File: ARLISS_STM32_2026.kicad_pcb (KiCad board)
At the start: 2 copper layers, 32 parts, among them J1 Conn_01x06, J2 Conn_01x06, U14 XL4005, U15 XC6220B331MR, U3 4754

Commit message: AVANCE 06
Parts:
- added SW1: SWITCH_BLACK, ARLISS-footprints:SW-TH_XKB_SS-12M11XX, F.Cu at (180.4, 115.3)
- added SW2: SWITCH_BLACK, ARLISS-footprints:SW-TH_XKB_SS-12M11XX, F.Cu at (179.0, 132.9)
- added U16: AP64501SP-13, ARLISS-footprints:SOIC-8_L4.9-W3.9-P1.27-LS6.0-BL-EP-1, F.Cu at (194.2, 100.8)

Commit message: feat: [solución de rules checker]
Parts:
- U14: value XL4005 -> XL4005E1
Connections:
- net GND renamed nFAULT2
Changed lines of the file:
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@@
 			(layers "F.Cu" "F.Mask" "F.Paste")
 			(roundrect_rratio 0.208333)
-			(net "GND")
+			(net "nFAULT2")
 			(pinfunction "A_1")
 			(pintype "passive")
@@
 			(layers "F.Cu" "F.Mask" "F.Paste")
 			(roundrect_rratio 0.208333)
-			(net "GND")
+			(net "nFAULT2")
 			(pinfunction "A_3")
 			(pintype "passive")
@@
 			(layers "F.Cu" "F.Mask" "F.Paste")
 			(roundrect_rratio 0.25)
-			(net "GND")
+			(net "nFAULT2")
 			(pintype "passive")
 		)
@@
 			(layers "F.Cu" "F.Mask" "F.Paste")
 			(roundrect_rratio 0.25)
-			(net "GND")
+			(net "nFAULT2")
 			(pintype "passive")
 		)
@@
 			(layers "F.Cu" "F.Mask" "F.Paste")
 			(roundrect_rratio 0.15625)
-			(net "GND")
+			(net "nFAULT2")
 			(pintype "passive")
 		)
@@
 			(size 1.5 1.5)
 			(layers "F.Cu" "F.Mask")
-			(net "GND")
+			(net "nFAULT2")
 			(pinfunction "1_1")
 			(pintype "passive")
@@
 			(layers "*.Cu" "*.Mask")
 			(remove_unused_layers no)
-			(net "GND")
+			(net "nFAULT2")
 			(pinfunction "Pin_5_5")
 			(pintype "passive")
@@
 			(layers "F.Cu" "F.Mask" "F.Paste")
 			(roundrect_rratio 0.25)
-			(net "GND")
+			(net "nFAULT2")
 			(pintype "passive")
 		)
@@
 			(layers "F.Cu" "F.Mask" "F.Paste")
 			(roundrect_rratio 0.25)
-			(net "GND")
+			(net "nFAULT2")
 			(pintype "passive")
 		)
@@
 			(layers "*.Cu" "*.Mask")
 			(remove_unused_layers no)
-			(net "GND")
+			(net "nFAULT2")
 			(pinfunction "3_3")
 			(pintype "unspecified")
@@
 			(layers "F.Cu" "F.Mask" "F.Paste")
 			(roundrect_rratio 0.25)
-			(net "GND")
+			(net "nFAULT2")
 			(pintype "passive")
 		)
@@
 			(layers "*.Cu" "*.Mask")
 			(remove_unused_layers no)
-			(net "GND")
+			(net "nFAULT2")
 			(pinfunction "Pin_2_2")
 			(pintype "passive")
@@
 			(layers "F.Cu" "F.Mask" "F.Paste")
 			(roundrect_rratio 0.25)
-			(net "GND")
+			(net "nFAULT2")
 			(pintype "passive")
 		)
@@
 			(layers "F.Cu" "F.Mask" "F.Paste")
 			(roundrect_rratio 0.25)
-			(net "GND")
+			(net "nFAULT2")
 			(pintype "passive")
 		)
@@
 			)
 		)
-		(property "Value" "XL4005"
+		(property "Value" "XL4005E1"
 			(at 0 6.65 0)
 			(layer "F.Fab")
@@
 			)
 		)
-		(property "Datasheet" "http://www.xlsemi.net/datasheet/XL4015%20datasheet-English.pdf"
+		(property "Datasheet" "https://lcsc.com/product-detail/DC-DC-Converters_XL4005E1_C73332.html"
 			(at 0 0 0)
 			(layer "F.Fab")
@@
 			)
 		)
-		(property "Description" "5A 180kHz 36V Buck DC to DC Converter"
+		(property "Description" ""
 			(at 0 0 0)
 			(layer "F.Fab")
@@
 			)
 		)
-		(property ki_fp_filters "TO?263*")
+		(property "Manufacturer" "XLSEMI(芯龙)"
+			(at 0 0 0)
+			(unlocked yes)
+			(layer "F.Fab")
+			(hide yes)
+			(effects
+				(font
+					(size 1 1)
+					(thickness 0.15)
+				)
+			)
+		)
+		(property "MPN" "XL4005E1"
+			(at 0 0 0)
+			(unlocked yes)
+			(layer "F.Fab")
+			(hide yes)
+			(effects
+				(font
+					(size 1 1)
+					(thickness 0.15)
+				)
+			)
+		)
+		(property "LCSC Part" "C73332"
+			(at 0 0 0)
+			(unlocked yes)
+			(layer "F.Fab")
+			(hide yes)
+			(effects
+				(font
+					(size 1 1)
+					(thickness 0.15)
+				)
+			)
+		)
 		(sheetname "/Alimentacion/")
 		(sheetfile "untitled.kicad_sch")
@@
 			(unit
 				(name "A")
-				(pins "5" "4" "1" "3" "2")
+				(pins "3" "6" "5" "4" "2" "1")
 			)
 		)
-		(attr smd)
+		(attr smd dnp)
 		(duplicate_pad_numbers_are_jumpers no)
 		(fp_line
@@
 			(layers "F.Cu" "F.Mask" "F.Paste")
 			(roundrect_rratio 0.227273)
-			(net "GND")
+			(net "nFAULT2")
 			(pinfunction "GND_1")
-			(pintype "power_in")
+			(pintype "unspecified")
 		)
 		(pad "2" smd roundrect
@@
 			(net "/Alimentacion/FB")
 			(pinfunction "FB_2")
-			(pintype "input")
+			(pintype "unspecified")
 		)
 		(pad "3" smd roundrect
@@
 			(net "/Alimentacion/SW")
 			(pinfunction "SW_3")
-			(pintype "power_out")
+			(pintype "unspecified")
 		)
 		(pad "3" smd roundrect
@@
 			(net "/Alimentacion/SW")
 			(pinfunction "SW_3")
-			(pintype "power_out")
+			(pintype "unspecified")
 		)
 		(pad "4" smd roundrect
@@
 			(roundrect_rratio 0.227273)
 			(net "+VIN")
-			(pinfunction "VC_4")
-			(pintype "input")
+			(pinfunction "EN_4")
+			(pintype "unspecified")
 		)
 		(pad "5" smd roundrect
@@
 			(net "+VIN")
 			(pinfunction "VIN_5")
-			(pintype "power_in")
+			(pintype "unspecified")
 		)
 		(embedded_fonts no)
@@
 			(layers "*.Cu" "*.Mask")
 			(remove_unused_layers no)
-			(net "GND")
+			(net "nFAULT2")
 			(pinfunction "3_3")
 			(pintype "unspecified")
@@
 			(layers "F.Cu" "F.Mask" "F.Paste")
 			(roundrect_rratio 0.15625)
-			(net "GND")
+			(net "nFAULT2")
 			(pintype "passive")
 		)
@@
 			(layers "F.Cu" "F.Mask" "F.Paste")
 			(roundrect_rratio 0.25)
-			(net "GND")
+			(net "nFAULT2")
 			(pintype "passive")
 		)
@@
 			(layers "F.Cu" "F.Mask" "F.Paste")
 			(roundrect_rratio 0.25)
-			(net "GND")
+			(net "nFAULT2")
 			(pintype "passive")
 		)
@@
 			(net "+5V")
 			(pinfunction "VIN_JP1_1")
-			(pintype "input")
+			(pintype "output")
 			(solder_mask_margin 0.102)
 		)
@@
 			(layers "*.Cu" "*.Mask")
 			(remove_unused_layers no)
-			(net "GND")
+			(net "nFAULT2")
 			(pinfunction "GND_JP1_3")
 			(pintype "power_in")
@@
 			(layers "F.Cu" "F.Mask" "F.Paste")
 			(roundrect_rratio 0.25)
-			(net "GND")
+			(net "nFAULT2")
 			(pintype "passive")
 		)
@@
 			(layers "F.Cu" "F.Mask" "F.Paste")
 			(roundrect_rratio 0.25)
-			(net "GND")
+			(net "nFAULT2")
 			(pinfunction "GND_2")
 			(pintype "power_in")
@@
 			(layers "F.Cu" "F.Mask" "F.Paste")
 			(roundrect_rratio 0.25)
-			(net "GND")
+			(net "nFAULT2")
 			(pintype "passive")
 		)
@@
 			(layers "F.Cu" "F.Mask" "F.Paste")
 			(roundrect_rratio 0.25)
-			(net "GND")
+			(net "nFAULT2")
 			(pintype "passive")
 		)

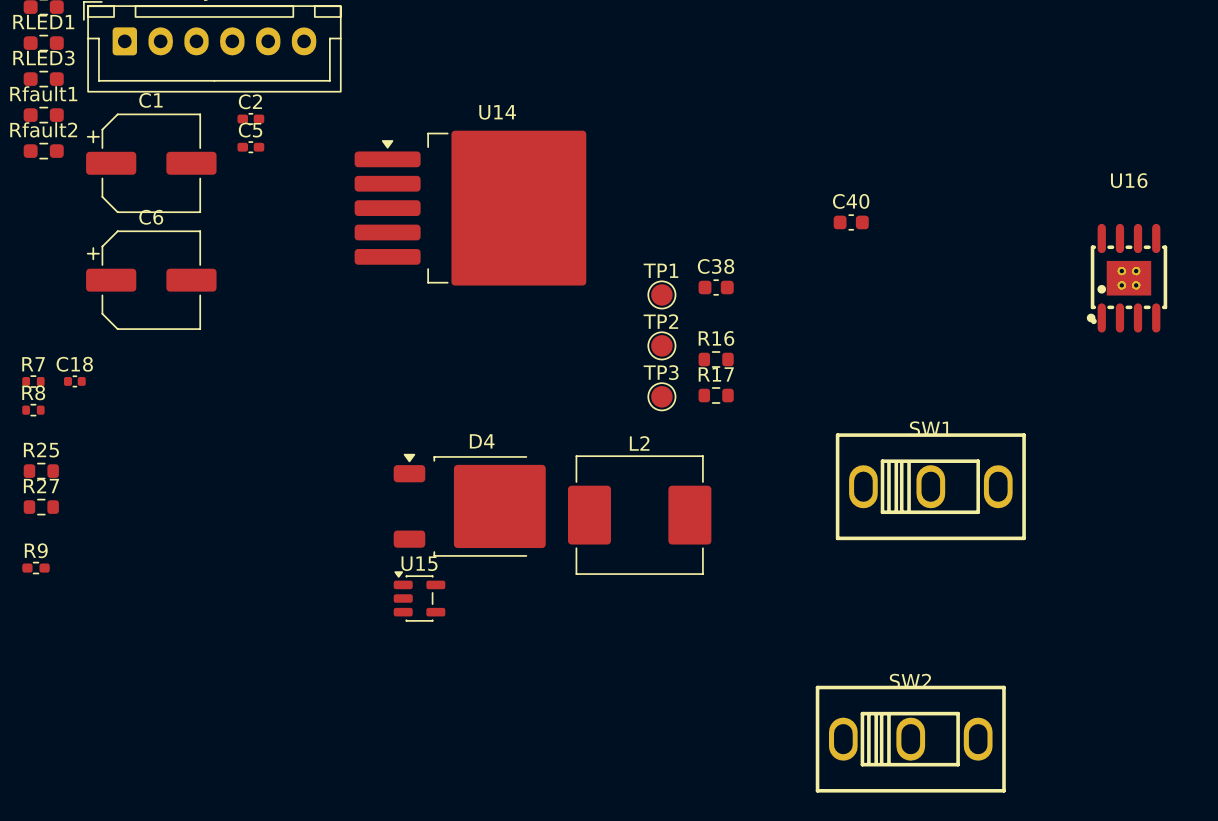
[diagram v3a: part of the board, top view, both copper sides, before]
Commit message: Footprints V2
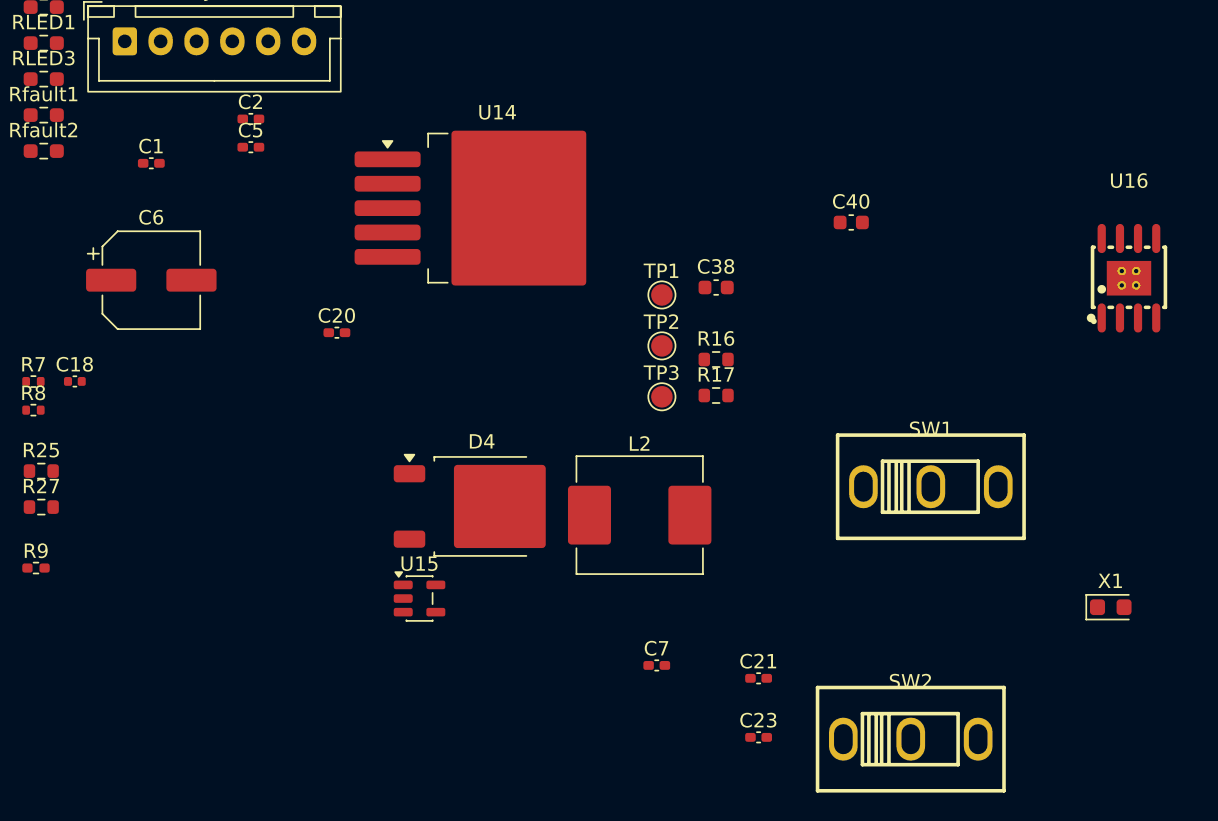
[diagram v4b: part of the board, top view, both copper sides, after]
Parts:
- added C20: 2.2uF, Capacitor_SMD:C_0402_1005Metric_Pad0.74x0.62mm_HandSolder, F.Cu at (139.0, 104.6)
- added C21: 2.2uF, Capacitor_SMD:C_0402_1005Metric_Pad0.74x0.62mm_HandSolder, F.Cu at (168.4, 128.7)
- added C23: 7p, Capacitor_SMD:C_0402_1005Metric_Pad0.74x0.62mm_HandSolder, F.Cu at (168.4, 132.8)
- added C7: 100nF, Capacitor_SMD:C_0402_1005Metric_Pad0.74x0.62mm_HandSolder, F.Cu at (161.3, 127.8)
- added X1: 32.768kHz 7pF SMD, Crystal:Crystal_SMD_2012-2Pin_2.0x1.2mm_HandSoldering, F.Cu at (193.0, 123.7)
- C1: footprint Capacitor_SMD:CP_Elec_6.3x5.4 -> Capacitor_SMD:C_0402_1005Metric_Pad0.74x0.62mm_HandSolder

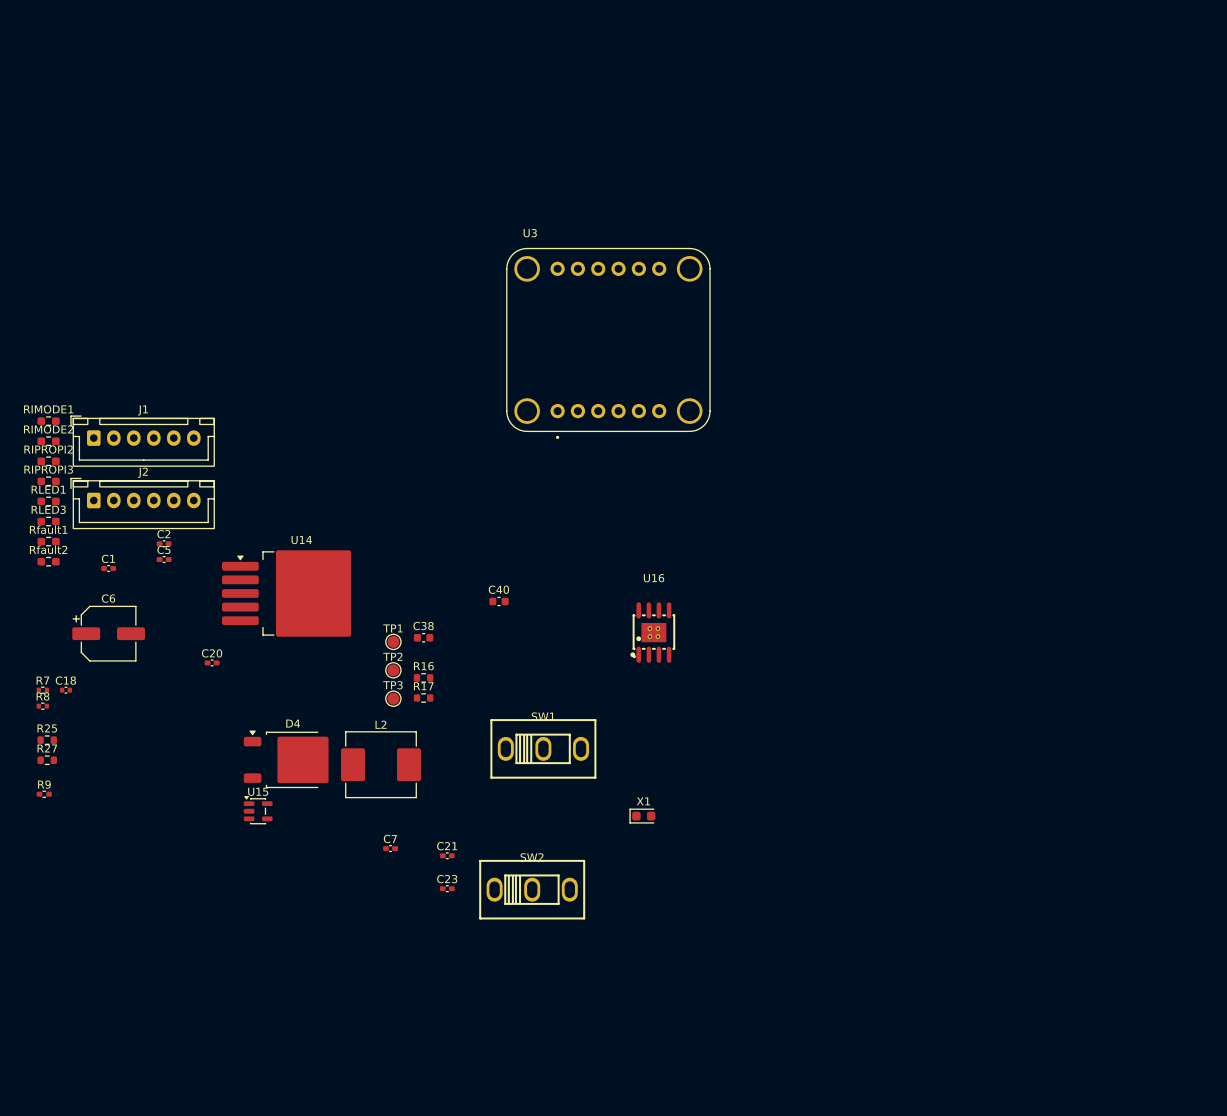
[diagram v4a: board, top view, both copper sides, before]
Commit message: Cantidad de errores en la placa: 04
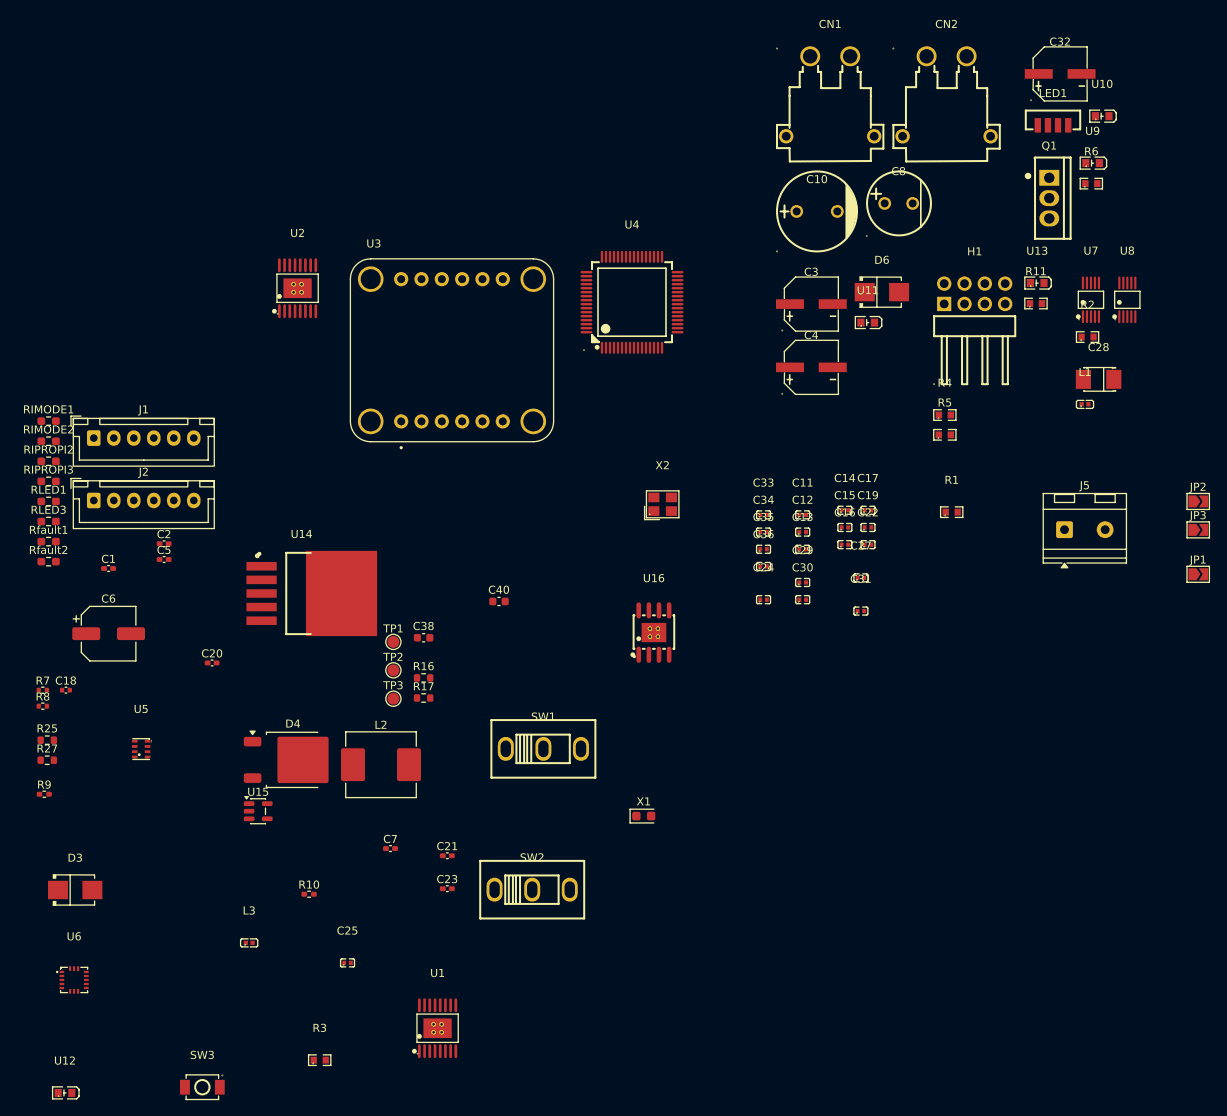
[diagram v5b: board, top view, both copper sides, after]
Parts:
- added C10: 330uF, ARLISS-footprints:CAP-TH_BD10.0-P5.00-D1.0-FD, F.Cu at (214.6, 48.1)
- added C11: 7pF, ARLISS-footprints:C0402, F.Cu at (212.8, 86.1)
- added C12: 10pF, ARLISS-footprints:C0402, F.Cu at (212.8, 88.2)
- added C13: 10pF, ARLISS-footprints:C0402, F.Cu at (212.8, 90.4)
- added C14: 100nF, ARLISS-footprints:C0402, F.Cu at (218.1, 85.5)
- added C15: 100nF, ARLISS-footprints:C0402, F.Cu at (218.1, 87.7)
- added C16: 100nF, ARLISS-footprints:C0402, F.Cu at (218.1, 89.8)
- added C17: 100nF, ARLISS-footprints:C0402, F.Cu at (221.0, 85.5)
- added C19: 1uF, ARLISS-footprints:C0402, F.Cu at (221.0, 87.7)
- added C22: 100nF, ARLISS-footprints:C0402, F.Cu at (221.0, 89.8)
- added C24: 100nF, ARLISS-footprints:C0402, F.Cu at (207.9, 96.7)
- added C25: 100nF, ARLISS-footprints:C0402, F.Cu at (155.9, 142.1)
- added C27: 100nF, ARLISS-footprints:C0402, F.Cu at (220.1, 94.0)
- added C28: 1uF, ARLISS-footprints:CAP-SMD_L3.5-W2.8-R-RD, F.Cu at (249.8, 69.1)
- added C29: 100nF, ARLISS-footprints:C0402, F.Cu at (212.8, 94.5)
- added C3: 100uF, ARLISS-footprints:CAP-SMD_BD6.3-L6.6-W6.6-FD, F.Cu at (213.9, 59.7)
- added C30: 100nF, ARLISS-footprints:C0402, F.Cu at (212.8, 96.7)
- added C31: 100nF, ARLISS-footprints:C0402, F.Cu at (220.1, 98.1)
- added C32: 10uF, ARLISS-footprints:CAP-SMD_BD6.3-L6.6-W6.6-LS7.3, F.Cu at (245.0, 31.0)
- added C33: 100nF, ARLISS-footprints:C0402, F.Cu at (207.9, 86.1)
- added C34: 100nF, ARLISS-footprints:C0402, F.Cu at (207.9, 88.2)
- added C35: 100nF, ARLISS-footprints:C0402, F.Cu at (207.9, 90.4)
- added C36: 100nF, ARLISS-footprints:C0402, F.Cu at (207.9, 92.5)
- added C4: 100uF, ARLISS-footprints:CAP-SMD_BD6.3-L6.6-W6.6-FD, F.Cu at (213.9, 67.6)
- added C8: 220uF, ARLISS-footprints:CAP-TH_BD8.0-P3.50-D0.6-FD, F.Cu at (224.8, 47.1)
- added CN1: XT30PW-M, ARLISS-footprints:CONN-TH_XT30PW-M, F.Cu at (216.3, 33.8)
- added CN2: XT30PW-M, ARLISS-footprints:CONN-TH_XT30PW-M, F.Cu at (230.8, 33.8)
- added D3: SMBJ18A_C151256, ARLISS-footprints:SMB_L4.3-W3.6-LS5.3-RD, F.Cu at (121.9, 133.0)
- added D6: SMBJ18A_C151256, ARLISS-footprints:SMB_L4.3-W3.6-LS5.3-RD, F.Cu at (222.7, 58.2)
- added H1: PZ254R-12-8P, ARLISS-footprints:HDR-TH_8P-P2.54-H-M-R2-C4-S2.54, F.Cu at (234.3, 58.4)
- added J5: Screw_Terminal_01x02, TerminalBlock_RND:TerminalBlock_RND_205-00232_1x02_P5.08mm_Horizontal, F.Cu at (245.6, 87.9)
- added JP1: SolderJumper_2_Open, Jumper:SolderJumper-2_P1.3mm_Open_TrianglePad1.0x1.5mm, F.Cu at (262.3, 93.5)
- added JP2: SolderJumper_2_Open, Jumper:SolderJumper-2_P1.3mm_Open_TrianglePad1.0x1.5mm, F.Cu at (262.3, 84.4)
- added JP3: SolderJumper_2_Open, Jumper:SolderJumper-2_P1.3mm_Open_TrianglePad1.0x1.5mm, F.Cu at (262.3, 88.0)
- added L1: 0R 100Mhz, ARLISS-footprints:L0402, F.Cu at (248.1, 72.3)
- added L3: 1Kohm_100Mhz, ARLISS-footprints:L0402, F.Cu at (143.6, 139.6)
- added LED1: VEML7700-TR, ARLISS-footprints:LED-SMD_4P-L6.8-W2.4_VEML7700-TR, F.Cu at (244.1, 37.4)
- added Q1: IRLZ44NPBF, ARLISS-footprints:TO-220-3_L10.0-W4.5-P2.54-T, F.Cu at (243.7, 46.5)
- added R1: 100k, ARLISS-footprints:R0603, F.Cu at (231.5, 85.7)
- added R10: 5.1K, Resistor_SMD:R_0402_1005Metric_Pad0.72x0.64mm_HandSolder, F.Cu at (151.1, 133.5)
- added R11: RC0603FR-7W10KL, ARLISS-footprints:R0603, F.Cu at (242.0, 59.7)
- added R2: 4.7K, ARLISS-footprints:R0603, F.Cu at (248.4, 63.8)
- added R3: 4.7K, ARLISS-footprints:R0603, F.Cu at (152.5, 154.2)
- added R4: 4.7K, ARLISS-footprints:R0603, F.Cu at (230.6, 73.6)
- added R5: 4.7K, ARLISS-footprints:R0603, F.Cu at (230.6, 76.1)
- added R6: 100k, ARLISS-footprints:R0603, F.Cu at (248.9, 44.7)
- added SW3: XDTD-0304-215, ARLISS-footprints:SW-SMD_L3.9-W3.0-P4.45, F.Cu at (137.8, 157.6)
- added U1: DRV8874PWPR, ARLISS-footprints:HTSSOP-16_L5.0-W4.4-P0.65-LS6.4-BL-EP, F.Cu at (167.2, 150.2)
- added U10: Green LED, ARLISS-footprints:LED0603-FD, F.Cu at (250.3, 36.2)
- added U11: Green LED, ARLISS-footprints:LED0603-FD, F.Cu at (221.0, 62.0)
- added U12: Green LED, ARLISS-footprints:LED0603-FD, F.Cu at (120.6, 158.3)
- added U13: Green LED, ARLISS-footprints:LED0603-FD, F.Cu at (242.2, 57.1)
- added U2: DRV8874PWPR, ARLISS-footprints:HTSSOP-16_L5.0-W4.4-P0.65-LS6.4-BL-EP, F.Cu at (149.7, 57.7)
- added U4: STM32F405RGT6, ARLISS-footprints:LQFP-64_L10.0-W10.0-P0.50-LS12.0-BL, F.Cu at (191.5, 59.5)
- added U5: DPS310XTSA1, ARLISS-footprints:LGA-8_DPS310XTSA1, F.Cu at (130.2, 115.3)
- added U6: ADXL372BCCZ-RL, ARLISS-footprints:LGA-16_L3.3-W3.0-P0.50-TL, F.Cu at (121.8, 144.2)
- added U7: INA226AIDGSR, ARLISS-footprints:MSOP-10_L3.0-W3.0-P0.50-LS5.0-BL, F.Cu at (248.9, 59.2)
- added U8: INA226AIDGSR, ARLISS-footprints:MSOP-10_L3.0-W3.0-P0.50-LS5.0-BL, F.Cu at (253.4, 59.2)
- added U9: Green LED, ARLISS-footprints:LED0603-FD, F.Cu at (249.1, 42.1)
- added X2: 8Mhz 10pF, ARLISS-footprints:CRYSTAL-SMD_4P-L3.2-W2.5-BL, F.Cu at (195.3, 84.8)
- U14: footprint Package_TO_SOT_SMD:TO-263-5_TabPin3 -> ARLISS-footprints:TO-263-5_L10.2-W9.2-P1.70-TL
- moved U3 19.6 mm to (169.0, 65.5)
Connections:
- J1 pad 1: /DriverDRV8874/M2- -> /Motor control/M2-
- J1 pad 6: /DriverDRV8874/M2+ -> /Motor control/M2+
- J2 pad 1: /DriverDRV8874/M1- -> /Motor control/M1-
- J2 pad 6: /DriverDRV8874/M1+ -> /Motor control/M1+
- RIMODE1 pad 1: /DriverDRV8874/IMODE1 -> /Motor control/IMODE1
- RIMODE2 pad 1: /DriverDRV8874/IMODE2 -> /Motor control/IMODE2
